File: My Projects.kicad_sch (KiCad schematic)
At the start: 4 parts

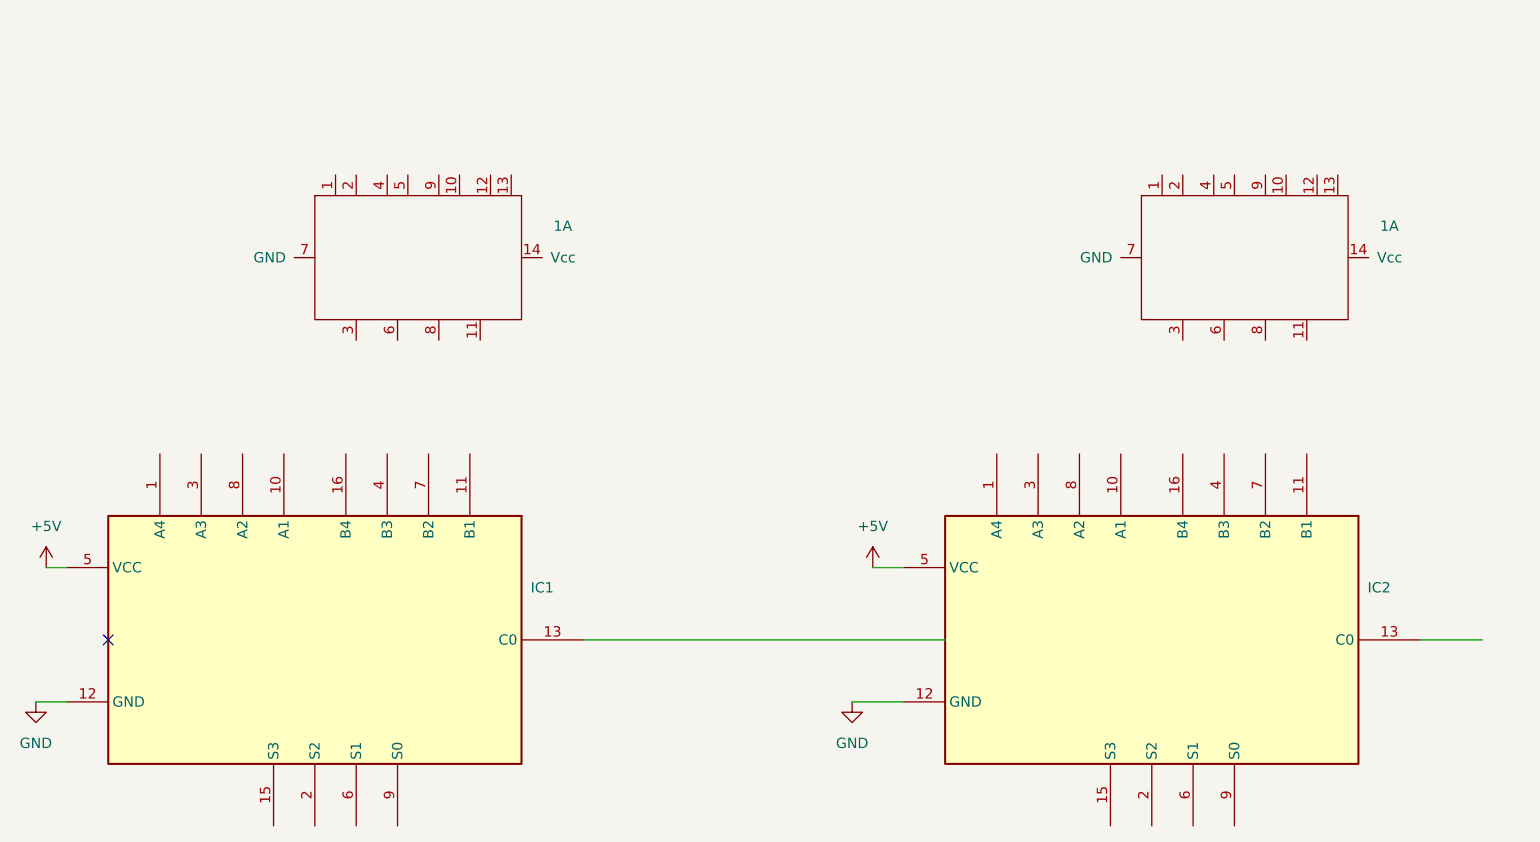
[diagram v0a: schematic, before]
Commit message: updated 7483
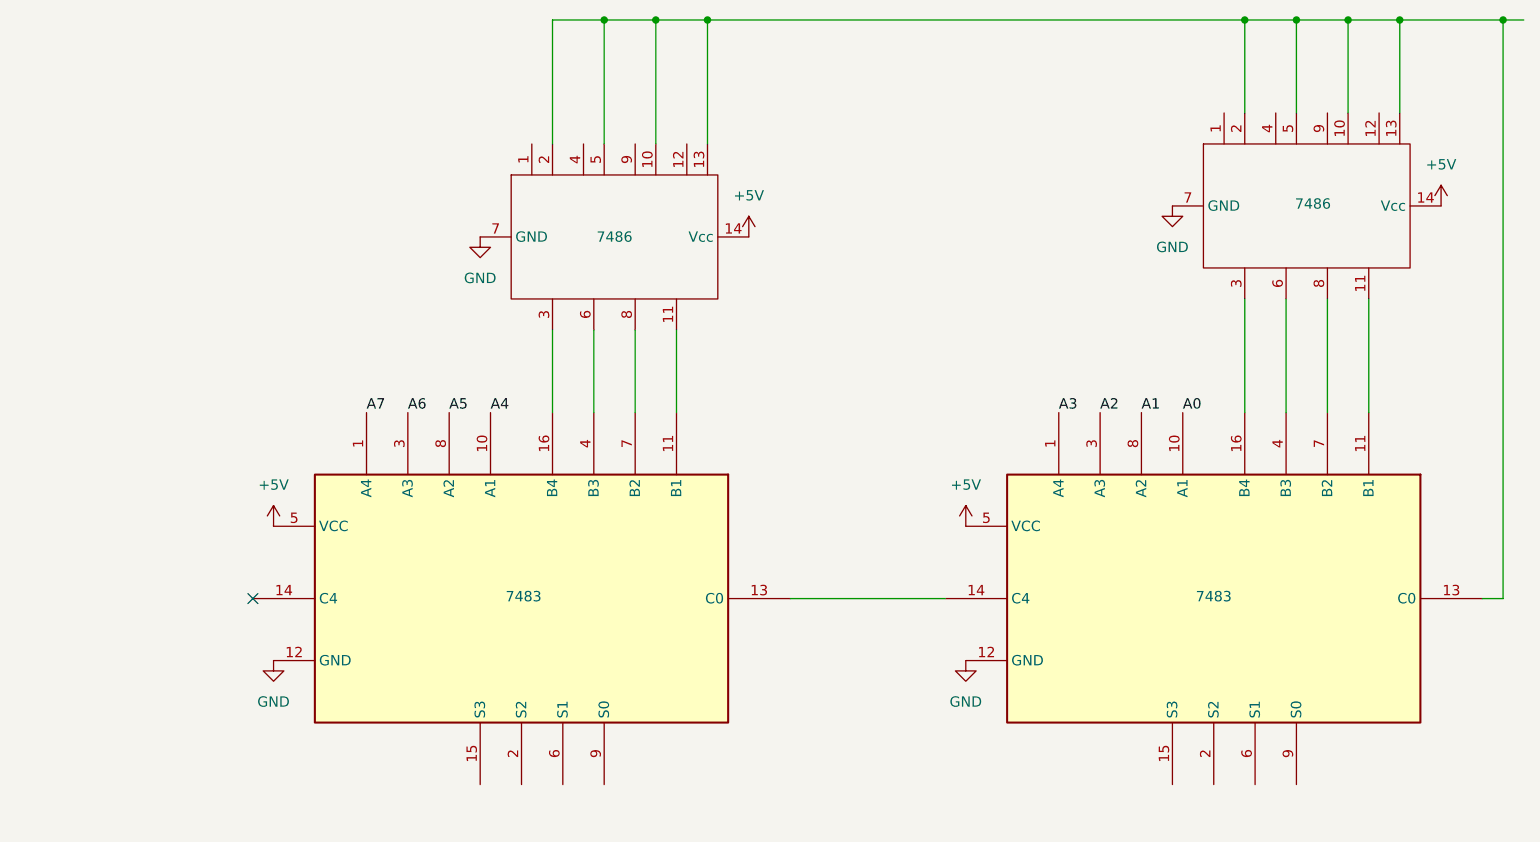
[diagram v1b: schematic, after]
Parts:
- removed 1 (x2): ~, symbol New_Library:NEW 7486
- added IC3, IC4: 7486, symbol New_Library:NEW 7486
- IC1, IC2: value ~ -> 7483
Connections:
- net +5V: now also IC3.14 (Vcc), IC4.14 (Vcc)
- net GND: now also IC3.7 (GND), IC4.7 (GND)
- net A7: now reaches IC1.1 (A4)
- net A4: now reaches IC1.10 (A1)
- net at IC1.11 (B1): now also IC3.11
- net at IC1.13 (C0): now also IC2.14 (C4); no longer IC2.
- net at IC1.16 (B4): now also IC3.3
- net A6: now reaches IC1.3 (A3)
- net at IC1.4 (B3): now also IC3.6
- net at IC1.7 (B2): now also IC3.8
- net A5: now reaches IC1.8 (A2)
- net A3: now reaches IC2.1 (A4)
- net A0: now reaches IC2.10 (A1)
- net at IC2.11 (B1): now also IC4.11
- net at IC2.13 (C0): now also IC3.10, IC3.13, IC3.2, IC3.5, IC4.10, IC4.13, IC4.2, IC4.5
- net at IC2.16 (B4): now also IC4.3
- net A2: now reaches IC2.3 (A3)
- net at IC2.4 (B3): now also IC4.6
- net at IC2.7 (B2): now also IC4.8
- net A1: now reaches IC2.8 (A2)
